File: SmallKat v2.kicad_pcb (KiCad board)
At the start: 4 copper layers, 100 x 56 mm, 159 parts, among them IC1 LMR14010A, IC2 LMR14010A, IC3 TPS40192DRCT-TPS40192DRCT, J1 Qwiic connector, J10 Conn_01x03_Male, J11 Conn_01x03_Male, J12 Conn_01x03_Male, J13 Conn_01x03_Male, J14 Conn_01x03_Male, J15 Conn_01x03_Male, J16 Conn_01x03_Male, J17 Conn_01x03_Male, J18 Conn_01x03_Male, J19 Conn_01x03_Male, J2 Qwiic connector, J20 Conn_01x03_Male, J21 Conn_01x03_Male, J22 Conn_01x03_Male, J23 Conn_01x03_Male, J24 Conn_01x03_Male, J25 Conn_01x02_Female, J26 Qwiic connector, J27 Qwiic connector, J28 Qwiic connector, J29 Qwiic connector, J3 Conn_01x03_Male, J4 Conn_01x03_Male, J5 Conn_01x03_Male, J6 Conn_01x03_Male, J7 Micro_SD_Card, J8 USB_C_Receptacle, J9 Conn_01x03_Male, Q1 MBT3904DW1, Q2 BUK9M17-30EX / BUK7M10-40E, Q3 BUK9M17-30EX / BUK7M10-40E, SW1 SW_SPST, SW2 SW_SPST, U1 PCA9685BS, U2 BNO055, U3 ESP32-WROOM-32, U4 CP2102N-A01-GQFN24, Y1 32.768kHz

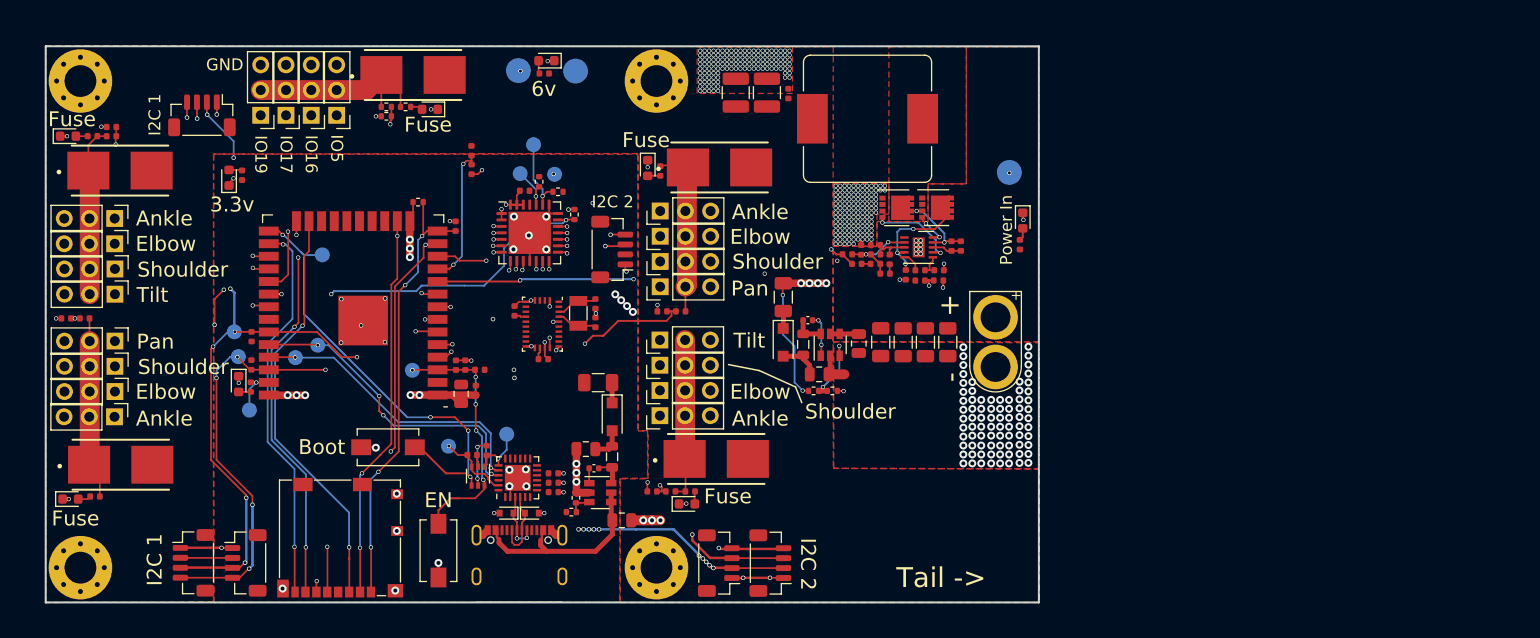
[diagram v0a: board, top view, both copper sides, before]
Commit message: added cm4
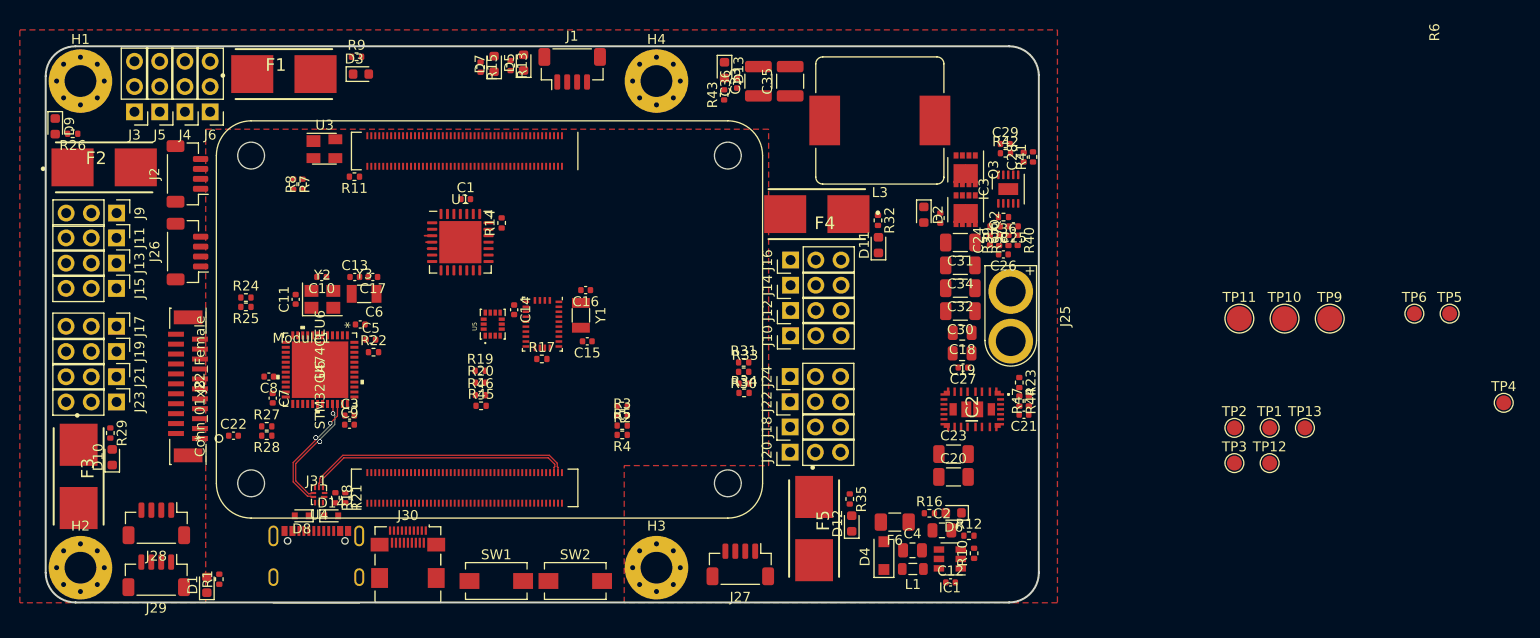
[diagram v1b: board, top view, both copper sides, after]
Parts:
- removed F7: Fuse, Fuse:Fuse_1206_3216Metric
- removed J7: Micro_SD_Card, Connector_Card:microSD_HC_Molex_104031-0811
- removed L2: 10uH, Inductor_SMD:L_0805_2012Metric
- removed Q1: MBT3904DW1, Package_TO_SOT_SMD:SOT-363_SC-70-6
- removed TP14, TP15, TP7, TP8: TestPoint, TestPoint:TestPoint_Pad_D1.5mm
- added C10: C, Capacitor_SMD:C_0402_1005Metric, F.Cu at (95.9, 105.0)
- added C11: C, Capacitor_SMD:C_0402_1005Metric, F.Cu at (93.3, 107.3)
- added C13: C, Capacitor_SMD:C_0402_1005Metric, F.Cu at (99.3, 105.0)
- added C7: C, Capacitor_SMD:C_0402_1005Metric, F.Cu at (91.0, 117.2)
- added C8: C, Capacitor_SMD:C_0402_1005Metric, F.Cu at (90.6, 115.1)
- added C9: C, Capacitor_SMD:C_0402_1005Metric, F.Cu at (98.7, 119.9)
- added D14: D_TVS, Diode_SMD:D_SOD-523, F.Cu at (96.9, 129.1)
- added J30: HDMI_A_1.4, Connector_HDMI:HDMI_Micro-D_Molex_46765-0x01, F.Cu at (104.6, 135.3)
- added J31: USB_C_Receptacle, C167321:C167321, F.Cu at (95.4, 133.2)
- added Module1: ComputeModule4-CM4, CM4IO:Raspberry-Pi-4-Compute-Module, F.Cu at (88.8, 92.8)
- added R15: R, Resistor_SMD:R_0402_1005Metric, F.Cu at (111.9, 83.9)
- added R47: R, Resistor_SMD:R_0402_1005Metric, F.Cu at (167.1, 117.5)
- added U5: ISM330DLCTR, ISM330DLCTR:PQFN50P250X300X86-14N, F.Cu at (113.2, 109.8)
- added U6: STM32G474CEU6, STM32G4:STM32G474CEU6, F.Cu at (95.8, 114.4)
- added Y2: Crystal_GND24_Small, Crystal:Crystal_SMD_Abracon_ABM8G-4Pin_3.2x2.5mm, F.Cu at (96.0, 107.3)
- added Y3: Crystal_Small, Crystal:Crystal_SMD_3215-2Pin_3.2x1.5mm, F.Cu at (100.2, 106.7)
- C17: value 22uF -> C; footprint Capacitor_SMD:C_0805_2012Metric -> Capacitor_SMD:C_0402_1005Metric
- C18: value 0.1uF -> C; footprint Capacitor_SMD:C_0402_1005Metric -> Capacitor_SMD:C_0805_2012Metric
- C19: value 4.7uF -> C; footprint Capacitor_SMD:C_0402_1005Metric -> Capacitor_SMD:C_0805_2012Metric
- C20, C23: value 0.1uF -> C; footprint Capacitor_SMD:C_0402_1005Metric -> Capacitor_SMD:C_1206_3216Metric
- C21, C3: value 0.1uF -> C
- C5: value 2.2uF -> C; footprint Capacitor_SMD:C_0805_2012Metric -> Capacitor_SMD:C_0402_1005Metric
- C6: value 10uF -> C; footprint Capacitor_SMD:C_0805_2012Metric -> Capacitor_SMD:C_0402_1005Metric
- D5: value DIODE -> LED; footprint Diode_SMD:D_SOD-123F -> LED_SMD:LED_0603_1608Metric
- D7: value D_TVS -> LED; footprint Diode_SMD:D_SOD-523 -> LED_SMD:LED_0603_1608Metric
- IC2: value LMR14010A -> TLVM13630; footprint Package_TO_SOT_SMD:SOT-23-6 -> TLVM13630:TLVM13630
- J25: footprint RC-Battery-Connectors:XT-60_male -> DJI_BATTERY_CONN:XT-30_female
- J8: value USB_C_Receptacle -> Conn_01x22_Female; footprint C167321:C167321 -> XF2J-222412A:XF2J-2224-12A
- R11: value 33.2 -> R
- R13, R18, R21, R22, R23, R44: value 10K -> R
- TP1, TP10, TP11, TP12, TP13, TP2, TP3, TP4, TP5, TP6, TP9: moved to F.Cu
- U3: value ESP32-WROOM-32 -> 74LVC1G07; footprint RF_Module:ESP32-WROOM-32 -> Package_TO_SOT_SMD:SOT-143
- U4: value CP2102N-A01-GQFN24 -> FSUSB42MX; footprint Package_DFN_QFN:QFN-24-1EP_4x4mm_P0.5mm_EP2.6x2.6mm -> Package_DFN_QFN:UQFN-10_1.4x1.8mm_P0.4mm
- moved TP5 116.3 mm to (209.5, 108.7)
- moved TP6 110.5 mm to (206.0, 108.7)
- moved TP1 102.7 mm to (191.4, 120.2)
- moved TP2 101.2 mm to (187.8, 120.2)
- moved TP3 100.9 mm to (187.8, 123.8)
- moved TP4 98.3 mm to (215.0, 117.7)
- moved TP13 82.7 mm to (194.9, 120.2)
- moved TP12 80.9 mm to (191.4, 123.8)
- moved D6 80.4 mm to (159.6, 128.8), turned to 180 degrees
- moved R16 77.1 mm to (157.1, 128.8), turned to 0 degrees
- moved TP11 76.8 mm to (188.3, 109.2)
- moved TP10 75.6 mm to (192.9, 109.2)
- moved R44 63.8 mm to (166.2, 117.5), turned to -90 degrees
- moved H2 58.0 mm to (71.7, 134.3)
- moved H4 58.0 mm to (129.7, 85.3)
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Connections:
- C17 pad 1: +3V3 -> Net-(C17-Pad1)
- C18 pad 1: +3V3 -> +BATT
- C19 pad 1: +3V3 -> +BATT
- C20 pad 1: +3V3 -> +5V
- C21 pad 2: +3V3 -> Net-(C21-Pad2)
- C22 pad 1: /MainBoard/ESP32Module/EN -> /MainBoard/ESP32Module/NRST
- C23 pad 1: /MainBoard/ESP32Module/EN -> +5V
- C3 pad 1: Net-(C3-Pad1) -> +3V3
- C3 pad 2: Net-(C3-Pad2) -> GND
- C5 pad 1: VBUS -> +3V3
- C6 pad 1: Net-(C6-Pad1) -> +3V3
- D5 pad 1: Net-(C6-Pad1) -> Net-(D5-Pad1)
- D5 pad 2: Net-(D5-Pad2) -> +3V3
- D7 pad 1: /MainBoard/ESP32Module/USBD_N -> Net-(D7-Pad1)
- D7 pad 2: GND -> +3V3
- D8 pad 1: /MainBoard/ESP32Module/USBD_P -> Net-(D8-Pad1)
- IC2 pad 1: Net-(C3-Pad2) -> /MainBoard/RT
- IC2 pad 2: GND -> +BATT
- IC2 pad 3: Net-(IC2-Pad3) -> +BATT
- IC2 pad 4: VBUS -> +BATT
- IC2 pad 5: VBUS -> GND
- IC2 pad 6: Net-(C3-Pad1) -> GND
- IC3 pad 1: (no net) -> unconnected-(IC3-Pad1)
- R1 pad 1: /MainBoard/ESP32Module/IO23 -> /MainBoard/ESP32Module/PB6
- R11 pad 1: +3V3 -> Net-(Module1-Pad99)
- R11 pad 2: Net-(IC2-Pad3) -> GND
- R13 pad 1: GND -> Net-(Module1-Pad21)
- R13 pad 2: Net-(IC2-Pad3) -> Net-(D5-Pad1)
- R18 pad 1: /MainBoard/IO12 -> /SEL
- R19 pad 1: /MainBoard/SCL -> /MainBoard/SDA
- R20 pad 1: /MainBoard/SDA -> /MainBoard/SCL
- R21 pad 1: Net-(Q1-Pad2) -> /SEL
- R21 pad 2: /MainBoard/ESP32Module/DTR -> Net-(J31-PadA4)
- R22 pad 1: Net-(Q1-Pad5) -> /BOOT0
- R22 pad 2: /MainBoard/ESP32Module/RTS -> GND
- R23 pad 1: +3V3 -> GND
- R23 pad 2: /MainBoard/ESP32Module/EN -> /MainBoard/RT
- R44 pad 1: /MainBoard/IO12 -> +5V
- R44 pad 2: GND -> Net-(IC2-Pad25)
- SW1 pad 1: GND -> Net-(Module1-Pad93)
- SW1 pad 2: /MainBoard/ESP32Module/IO0 -> GND
- SW2 pad 2: /MainBoard/ESP32Module/EN -> /MainBoard/ESP32Module/NRST
- TP1 pad 1: /MainBoard/ESP32Module/IO23 -> /MainBoard/ESP32Module/PB6
- TP5 pad 1: /MainBoard/ESP32Module/TXD -> Net-(TP5-Pad1)
- TP6 pad 1: /MainBoard/ESP32Module/RXD -> Net-(TP6-Pad1)
- U2 pad 1: (no net) -> unconnected-(U2-Pad1)
- U2 pad 10: (no net) -> unconnected-(U2-Pad10)
- U2 pad 11: (no net) -> /MainBoard/BNO055/RESET
- U2 pad 12: (no net) -> unconnected-(U2-Pad12)
- U2 pad 13: (no net) -> unconnected-(U2-Pad13)
- U2 pad 14: (no net) -> /MainBoard/BNO055/INT
- U2 pad 21: (no net) -> unconnected-(U2-Pad21)
- U2 pad 22: (no net) -> unconnected-(U2-Pad22)
- U2 pad 23: (no net) -> unconnected-(U2-Pad23)
- U2 pad 24: (no net) -> unconnected-(U2-Pad24)
- U2 pad 7: (no net) -> unconnected-(U2-Pad7)
- U2 pad 8: (no net) -> unconnected-(U2-Pad8)
- U3 pad 1: GND -> (no net)
- U3 pad 2: +3V3 -> Net-(Module1-Pad95)
- U3 pad 3: /MainBoard/ESP32Module/EN -> GND
- U3 pad 4: MEASURED_FUSE3 -> Net-(R15-Pad1)
- U4 pad 1: (no net) -> +3V3
- U4 pad 10: (no net) -> GND
- U4 pad 2: GND -> /SEL
- U4 pad 3: /MainBoard/ESP32Module/USBD_P -> /USB2_P
- U4 pad 4: /MainBoard/ESP32Module/USBD_N -> /USB2_N
- U4 pad 5: +3V3 -> GND
- U4 pad 6: +3V3 -> /USB_N
- U4 pad 7: +3V3 -> /USB_P
- U4 pad 8: +3V3 -> Net-(D8-Pad1)
- U4 pad 9: (no net) -> Net-(D14-Pad1)
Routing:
- net /MainBoard/SCL: track 95.0 -> 0.00 mm, vias 9 -> 0
- net /MainBoard/SDA: track 93.1 -> 0.00 mm, vias 8 -> 0
- net GND: track 91.6 -> 0.00 mm, vias 430 -> 0
- net /MainBoard/SCL_1: track 82.2 -> 0.00 mm, vias 5 -> 0
- net /MainBoard/SDA_1: track 79.6 -> 0.00 mm, vias 7 -> 0
- net +3V3: track 76.5 -> 0.00 mm, vias 23 -> 0
- net /MainBoard/BATT_VOLTAGE: track 53.5 -> 0.00 mm, vias 5 -> 0
- net /MainBoard/SERVO7: track 48.1 -> 0.00 mm, vias 1 -> 0
- net /MainBoard/SERVO6: track 46.5 -> 0.00 mm, vias 1 -> 0
- net /MainBoard/ESP32Module/IO0: track 45.4 -> 0.00 mm, vias 4 -> 0
- net /MainBoard/IO12: track 45.1 -> 0.00 mm, vias 4 -> 0
- net /MainBoard/SERVO5: track 44.7 -> 0.00 mm, vias 1 -> 0
- net MEASURED_FUSE1: track 44.3 -> 0.00 mm, vias 2 -> 0
- net /MainBoard/SERVO4: track 42.6 -> 0.00 mm, vias 1 -> 0
- net /MainBoard/SERVO3: track 42.5 -> 0.00 mm, vias 1 -> 0
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- removed copper zone on F.Cu, net +3V3
- removed copper zone on F.Cu, net +BATT
- removed copper zone on B.Cu, net GND
- removed copper zone on F.Cu, net GND
- removed copper zone on In2.Cu, net GND
- removed copper zone on F.Cu, net Net-(C29-Pad1)
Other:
- outline, holes or cut-outs redrawn
- net class Default removed
- board text removed: "+"
- board text removed: "-"
- board text removed: "3.3v"
- board text removed: "6v"
- board text removed: "Ankle"
- board text removed: "Batt"
- board text removed: "Board by: Keion Bisland 2021"
- board text removed: "Boot"
- board text removed: "DTR"
- board text removed: "EN"
- board text removed: "Elbow"
- board text removed: "Fuse"
- board text removed: "GND"
- board text removed: "Head ->"
- board text removed: "I2C 1"
- board text removed: "I2C 2"
- board text removed: "IO 23"
- board text removed: "IO0"
- board text removed: "IO16"
- board text removed: "IO17"
- board text removed: "IO19"
- board text removed: "IO5"
- board text removed: "Motherboard"
- board text removed: "Pan"
- board text removed: "Power In"
- board text removed: "RTS"
- board text removed: "RX"
- board text removed: "Rev 1.0"
- board text removed: "SCL"
- board text removed: "SCL 1"
- board text removed: "SDA"
- board text removed: "SDA 1"
- board text removed: "Shoulder"
- board text removed: "SmallKat"
- board text removed: "TX"
- board text removed: "Tail ->"
- board text removed: "Tilt"
